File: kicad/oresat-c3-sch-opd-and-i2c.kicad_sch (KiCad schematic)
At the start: 37 parts, among them Q1 NTR2101P, U12 RCLAMP0504FB, U13 MAX892LEUA+T, U24 RV-3028-C7, U30 FM24CL64B-DGTR, U37 LTC4300A-1

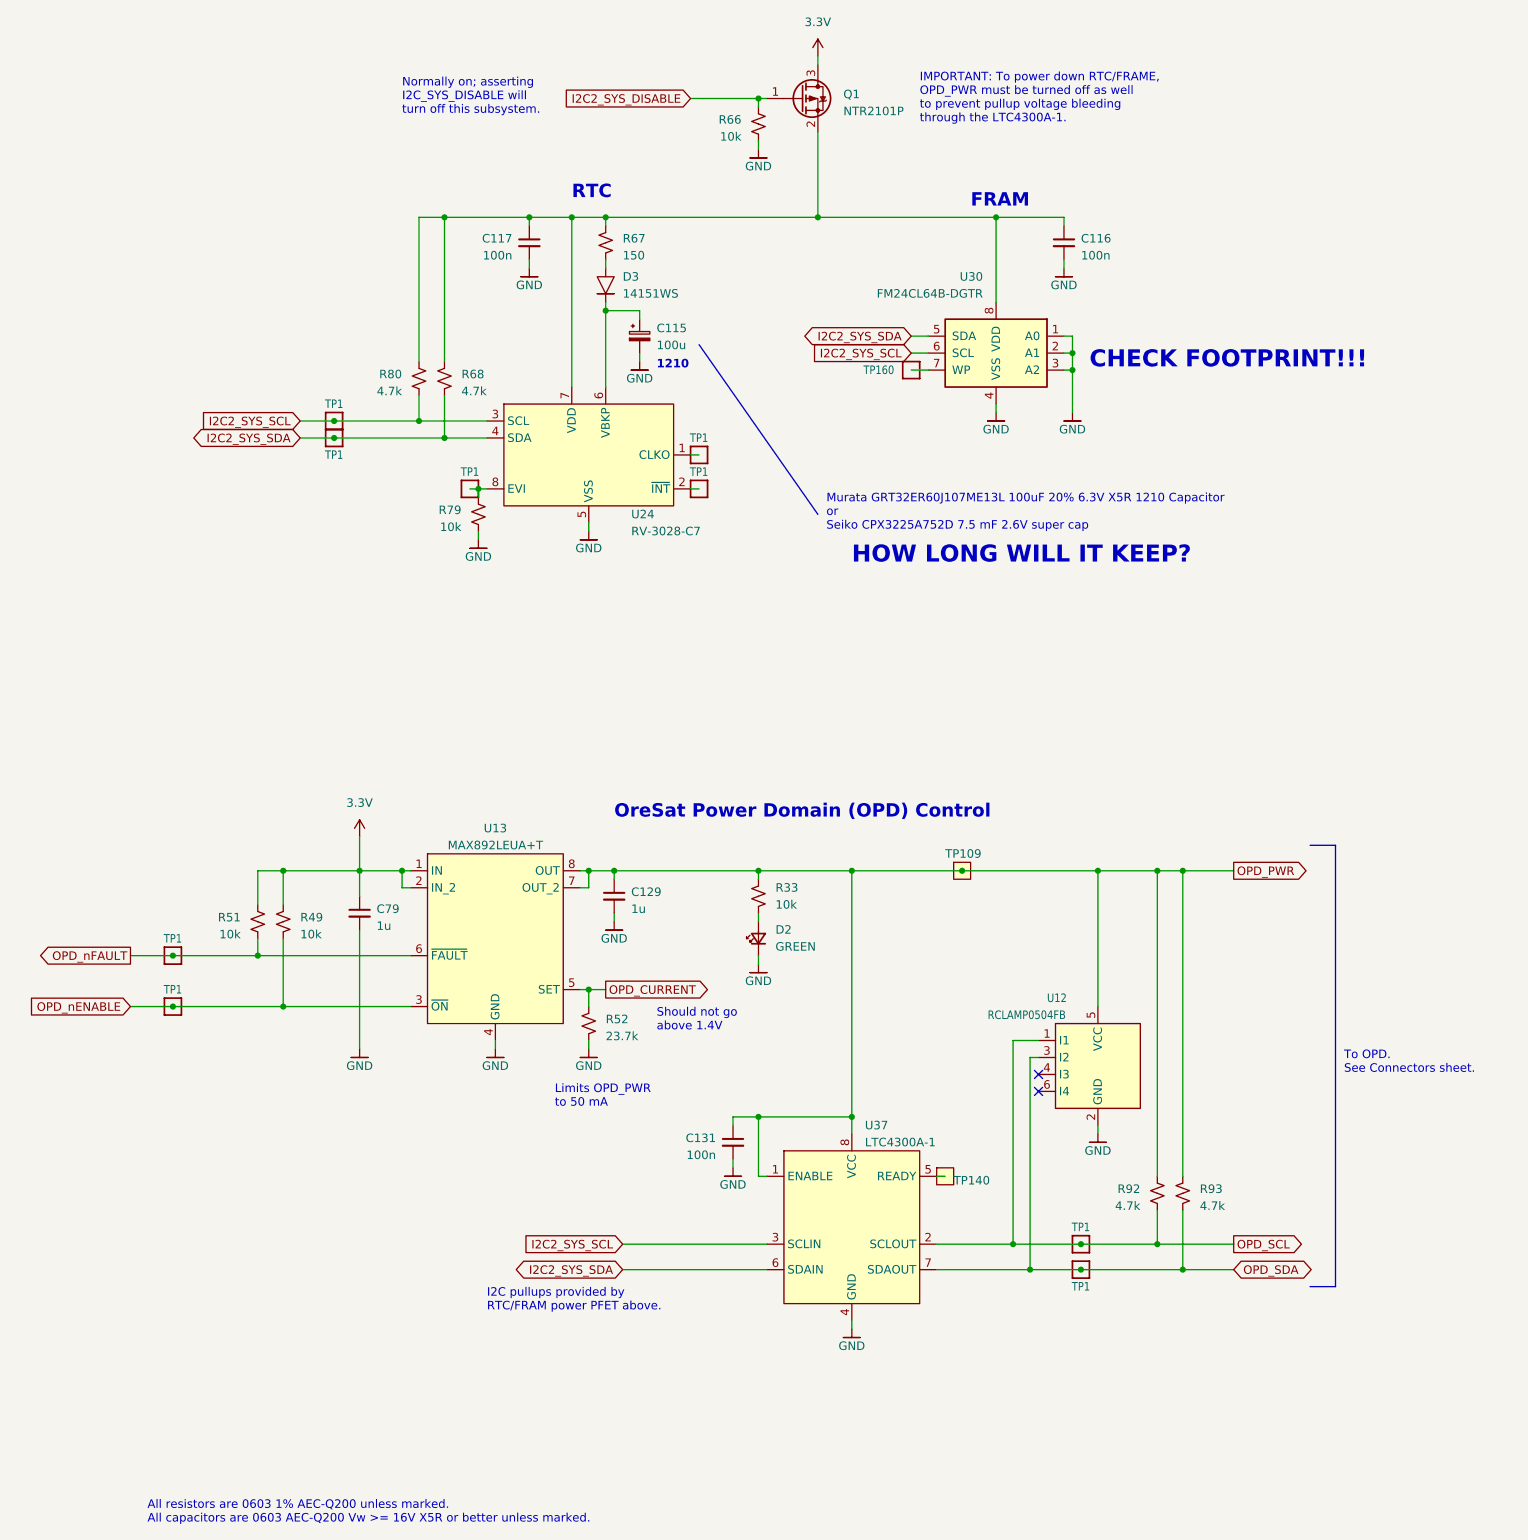
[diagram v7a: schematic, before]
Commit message: Fixed footprints and laid out WDT and OPD circuitry.
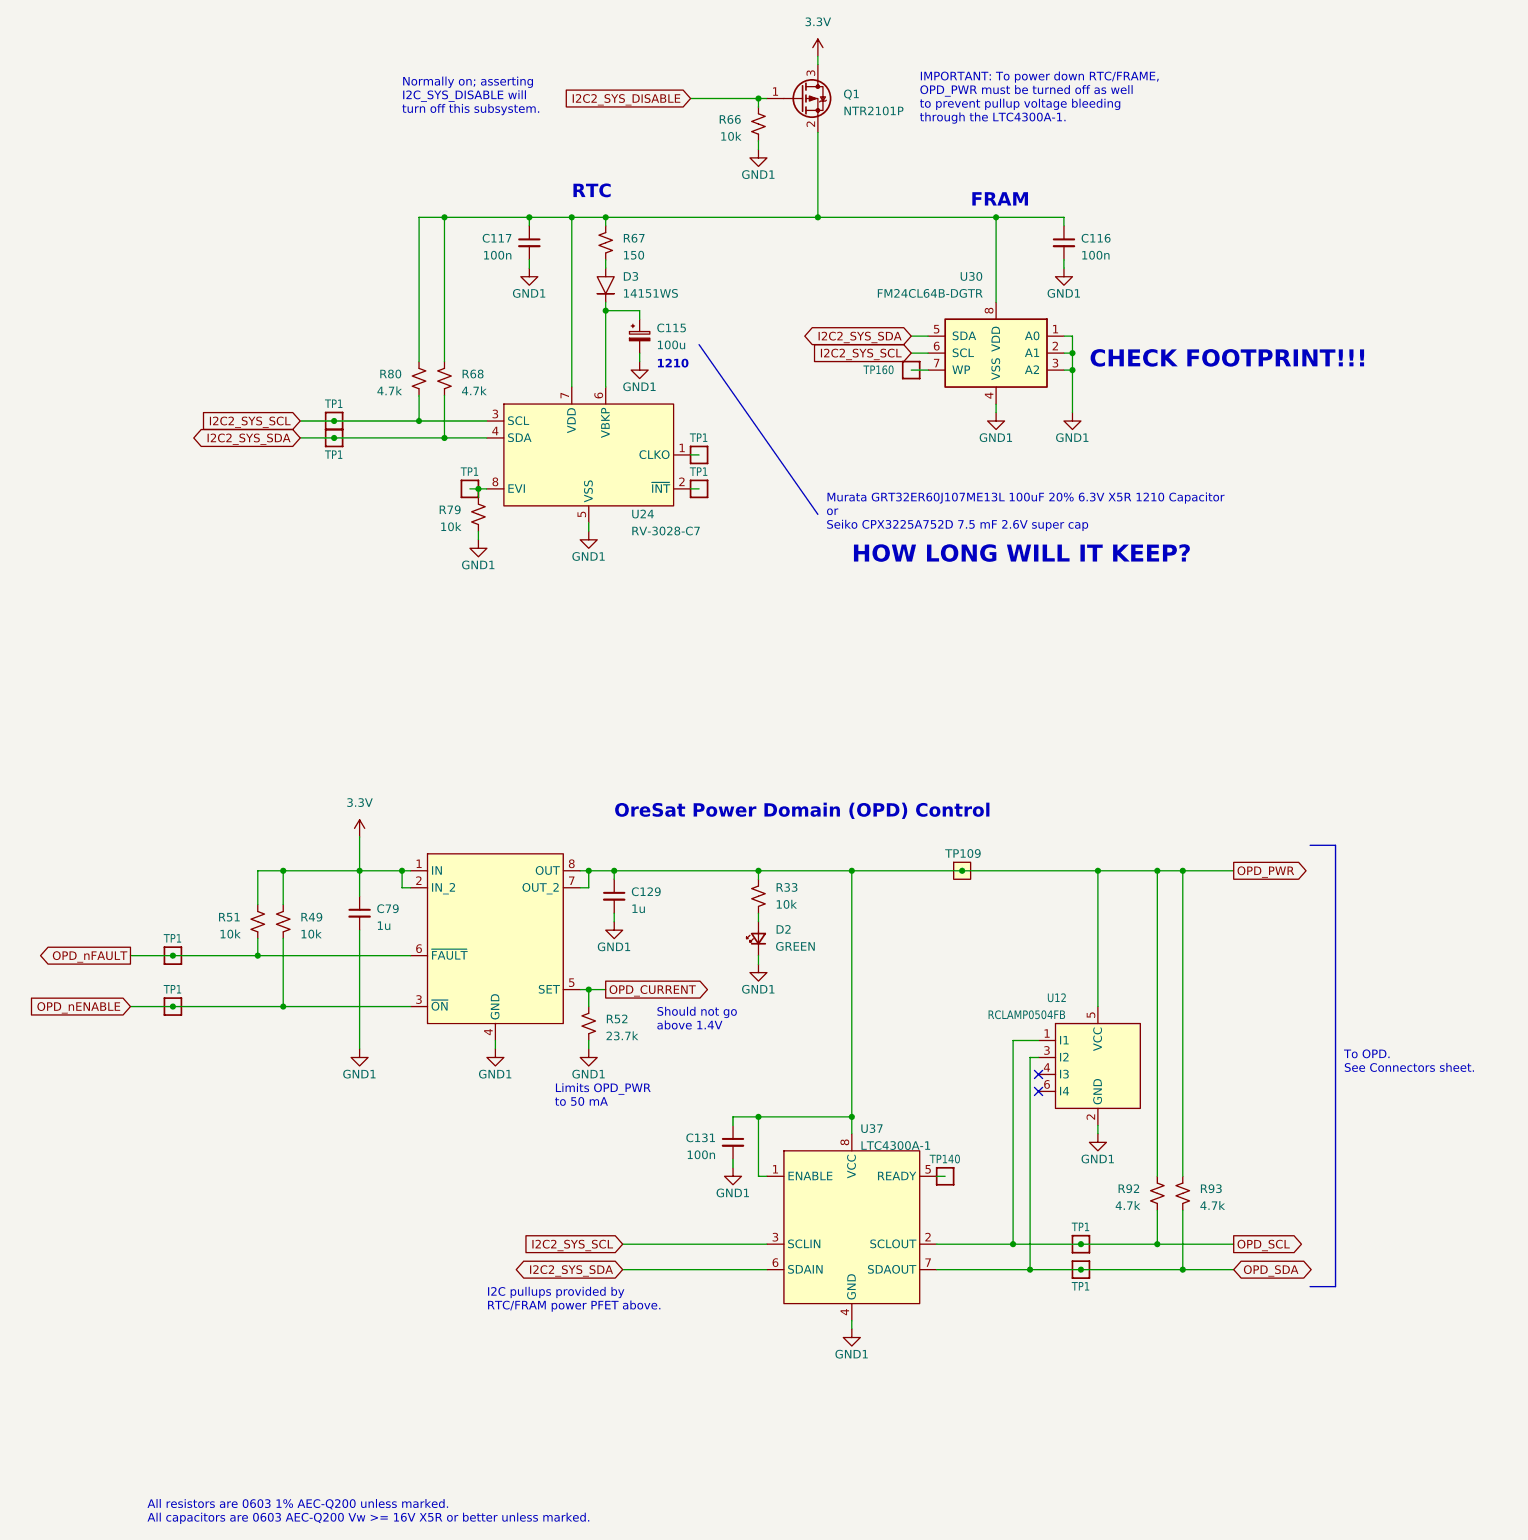
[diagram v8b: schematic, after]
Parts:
- C115: footprint (none) -> Capacitor_SMD:C_1210_3225Metric
- C116, C117, C129, C131, C79: footprint (none) -> Capacitor_SMD:C_0603_1608Metric
- R49, R51, R52, R66, R67, R68, R79, R80, R92, R93: footprint (none) -> Resistor_SMD:R_0603_1608Metric
- TP140: value TestPoint-MinTH -> ~; footprint oresat-misc:TestPoint-0.75mm-th -> oresat-misc:TestPoint_Pad_D1.0mm; symbol oresat-misc:Test-Point-0.75mm-th -> oresat-misc:Test-Point-1mm-round
- U13: footprint oresat-c3:21-0036K -> oresat-ics:LINEAR-MSOP-8-AND-MAXIM-UMAX-8-21-0036
- U37: footprint (none) -> oresat-ics:LINEAR-MSOP-8-AND-MAXIM-UMAX-8-21-0036
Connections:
- net at R67.2: now also D3.2; no longer D3. (2)
- net at C115.1, U24.6 (VBKP): now also D3.1; no longer D3. (2)
- net GND renamed GND1
